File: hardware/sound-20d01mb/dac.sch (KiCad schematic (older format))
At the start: 18 parts

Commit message: THT to SMD Capacitor
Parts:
- C?: footprint Capacitor_THT:CP_Radial_D8.0mm_P3.50mm -> Capacitor_SMD:CP_Elec_4x5.4
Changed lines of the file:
@@
 F 0 "C?" H 3468 4846 50  0000 L CNN
 F 1 "10uF" H 3468 4755 50  0000 L CNN
-F 2 "Capacitor_THT:CP_Radial_D8.0mm_P3.50mm" H 3388 4650 50  0001 C CNN
+F 2 "Capacitor_SMD:CP_Elec_4x5.4" H 3388 4650 50  0001 C CNN
 F 3 "~" H 3350 4800 50  0001 C CNN
 	1    3350 4800

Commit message: Added AD1938
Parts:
- removed C? (x2): 2.2uF, Capacitor_SMD:C_1206_3216Metric_Pad1.42x1.75mm_HandSolder, symbol Device:C
- removed C?: 10uF, Capacitor_THT:CP_Radial_D8.0mm_P3.50mm, symbol Device:CP
- removed C? (x2): 0.1uF, Capacitor_SMD:C_1206_3216Metric_Pad1.42x1.75mm_HandSolder, symbol Device:C
- removed U?: PCM5102A, Package_SO:TSSOP-20_4.4x6.5mm_P0.65mm, symbol sound-20d01_Library:PCM5102A
- added U?: AD1938, Package_QFP:LQFP-48_7x7mm_P0.5mm, symbol sound-20d01_Library:AD1938
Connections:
- wire segments 94 -> 44
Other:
- moved on the sheet: C?

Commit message: Updated schematics
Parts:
- added C?: 10uF, Capacitor_SMD:CP_Elec_4x5.4, symbol Device:CP
- added C? (x2): 0.1uF, Capacitor_SMD:C_1206_3216Metric_Pad1.42x1.75mm_HandSolder, symbol Device:C
- added C?: 47uF, symbol Device:CP
- added C?: 5.6nF, symbol Device:C
- added C?: 390pF, symbol Device:C
- added R?: 562R, symbol Device:R
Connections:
- net labels added: DAC_CM, DAC_FILTR, DAC_LF
- wire segments 44 -> 95
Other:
- moved on the sheet: C?, R?, U?

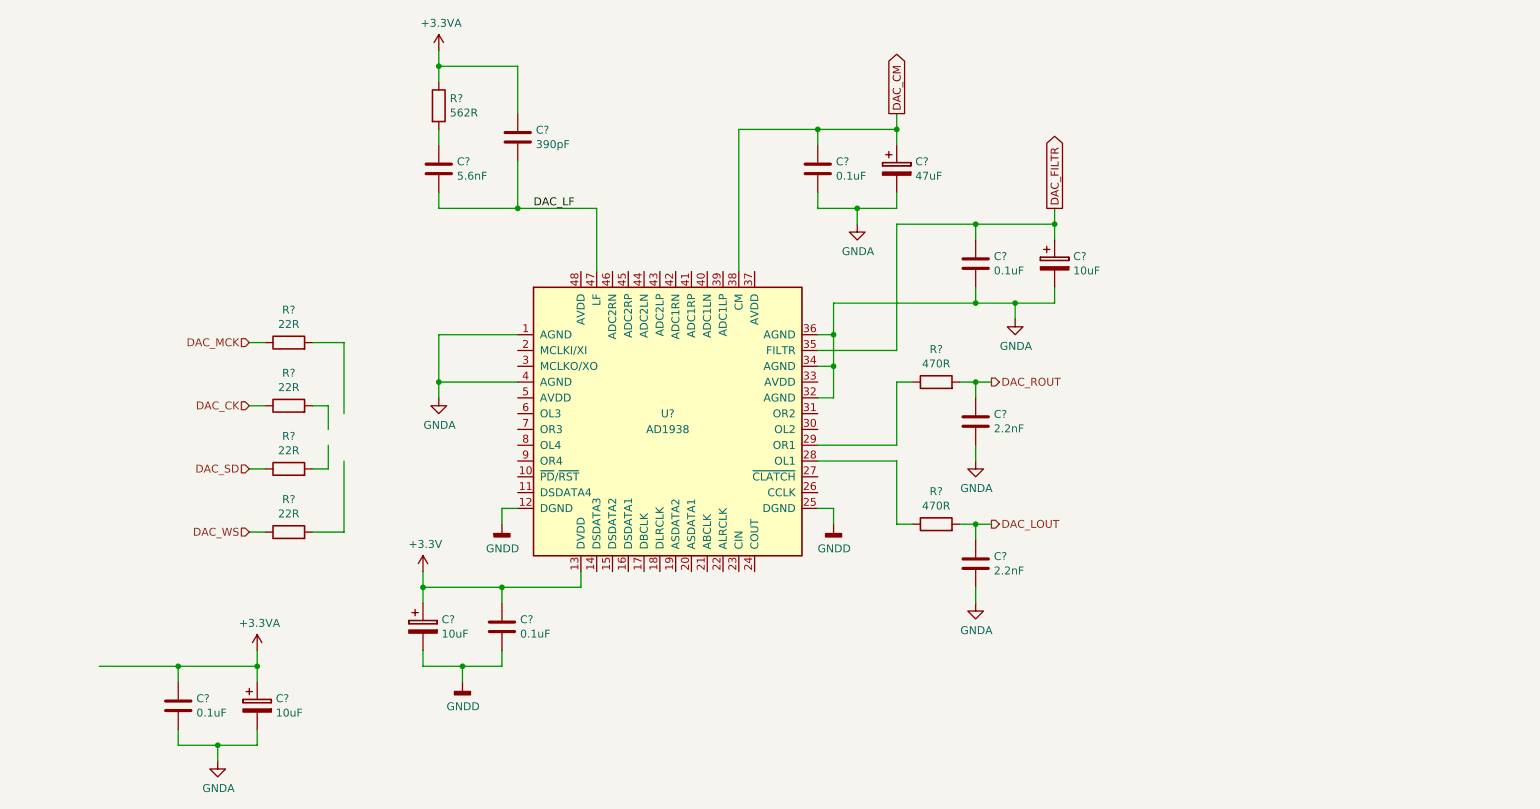
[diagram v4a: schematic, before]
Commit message: Added PCM5142
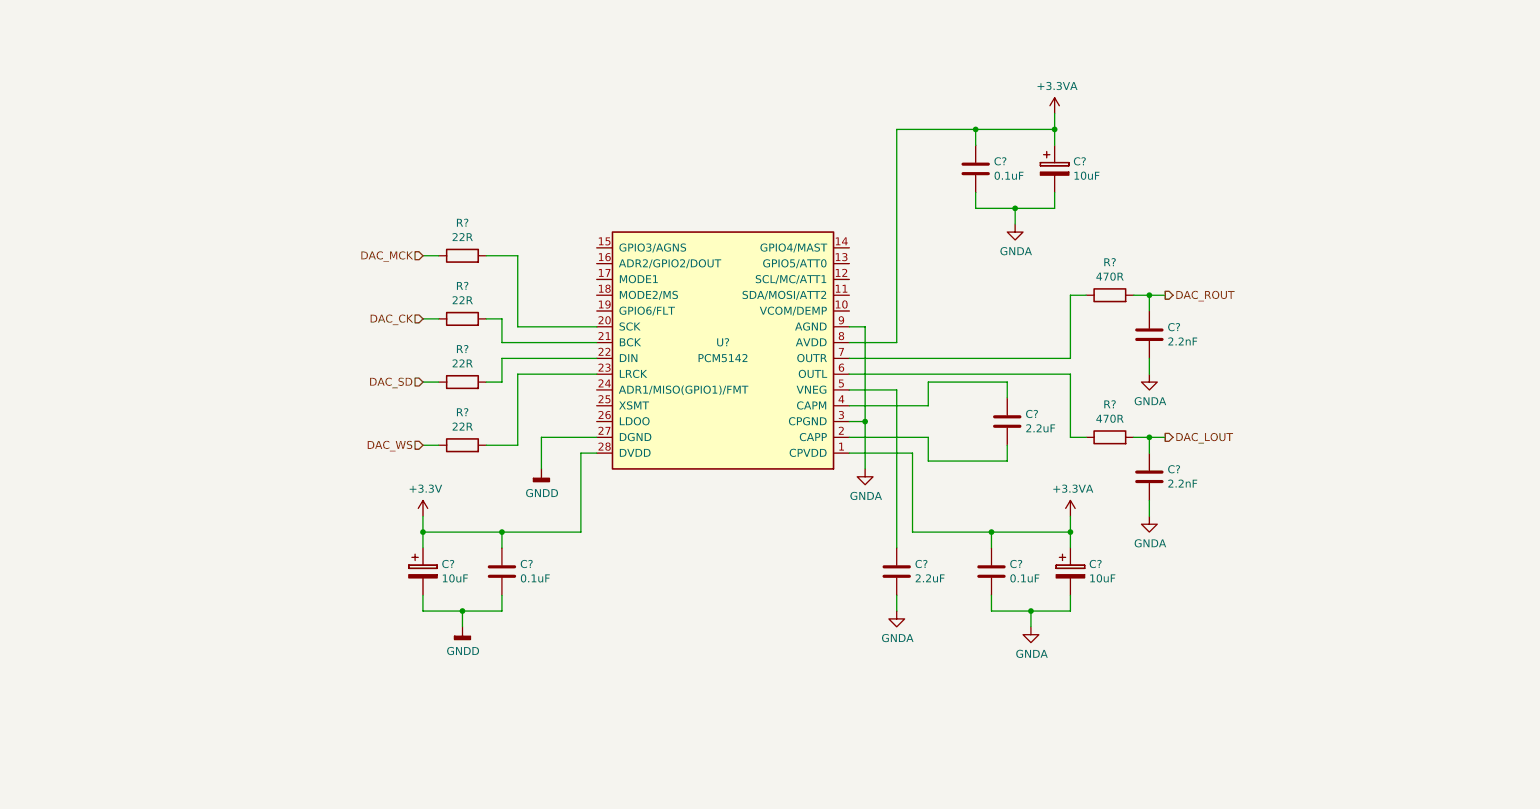
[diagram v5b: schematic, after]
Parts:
- removed C?: 10uF, Capacitor_SMD:CP_Elec_4x5.4, symbol Device:CP
- removed C? (x2): 0.1uF, Capacitor_SMD:C_1206_3216Metric_Pad1.42x1.75mm_HandSolder, symbol Device:C
- removed C?: 47uF, symbol Device:CP
- removed C?: 5.6nF, symbol Device:C
- removed C?: 390pF, symbol Device:C
- removed R?: 562R, symbol Device:R
- removed U?: AD1938, Package_QFP:LQFP-48_7x7mm_P0.5mm, symbol sound-20d01_Library:AD1938
- added C? (x2): 2.2uF, Capacitor_SMD:C_1206_3216Metric_Pad1.42x1.75mm_HandSolder, symbol Device:C
- added C?: 10uF, Capacitor_THT:CP_Radial_D8.0mm_P3.50mm, symbol Device:CP
- added C?: 0.1uF, Capacitor_SMD:C_1206_3216Metric_Pad1.42x1.75mm_HandSolder, symbol Device:C
- added U?: PCM5142, Package_SO:TSSOP-28_4.4x9.7mm_P0.65mm, symbol sound-20d01_Library:PCM5142
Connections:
- net labels removed: DAC_CM, DAC_FILTR, DAC_LF
- wire segments 95 -> 83
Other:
- moved on the sheet: C?, R?

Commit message: Added I2C Volume control
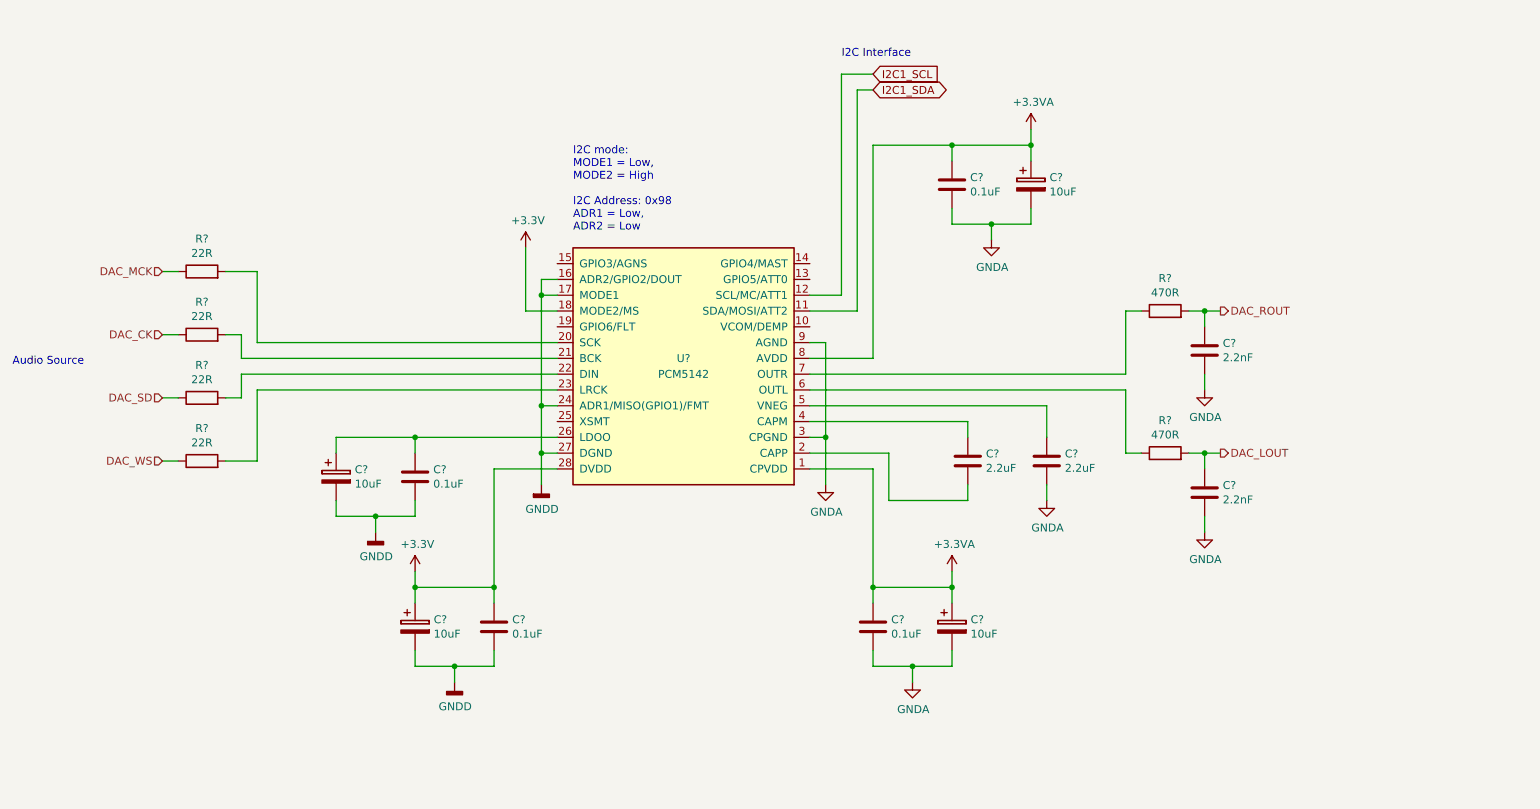
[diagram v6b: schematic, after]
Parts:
- added C?: 10uF, Capacitor_SMD:CP_Elec_4x5.4, symbol Device:CP
- added C?: 0.1uF, Capacitor_SMD:C_1206_3216Metric_Pad1.42x1.75mm_HandSolder, symbol Device:C
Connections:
- net +3V3: now also U?.18 (MODE2/MS)
- net GNDD: now also U?.16 (ADR2/GPIO2/DOUT), U?.17 (MODE1), U?.24 (ADR1/MISO(GPIO1)/FMT), C?.2, C?.2
- net I2C1_SDA: now reaches U?.11 (SDA/MOSI/ATT2)
- net I2C1_SCL: now reaches U?.12 (SCL/MC/ATT1)
- net at U?.26 (LDOO): now also C?.1, C?.1
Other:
- note added: "Audio Source"
- note added: "I2C Interface"
- note added: "I2C mode:\nMODE1 = Low,\nMODE2 = High\n\nI2C Address: 0x98\nADR1 = Low,\nADR2 = Low"
- moved on the sheet: C?, R?, U?

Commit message: Updated PSU and DAC
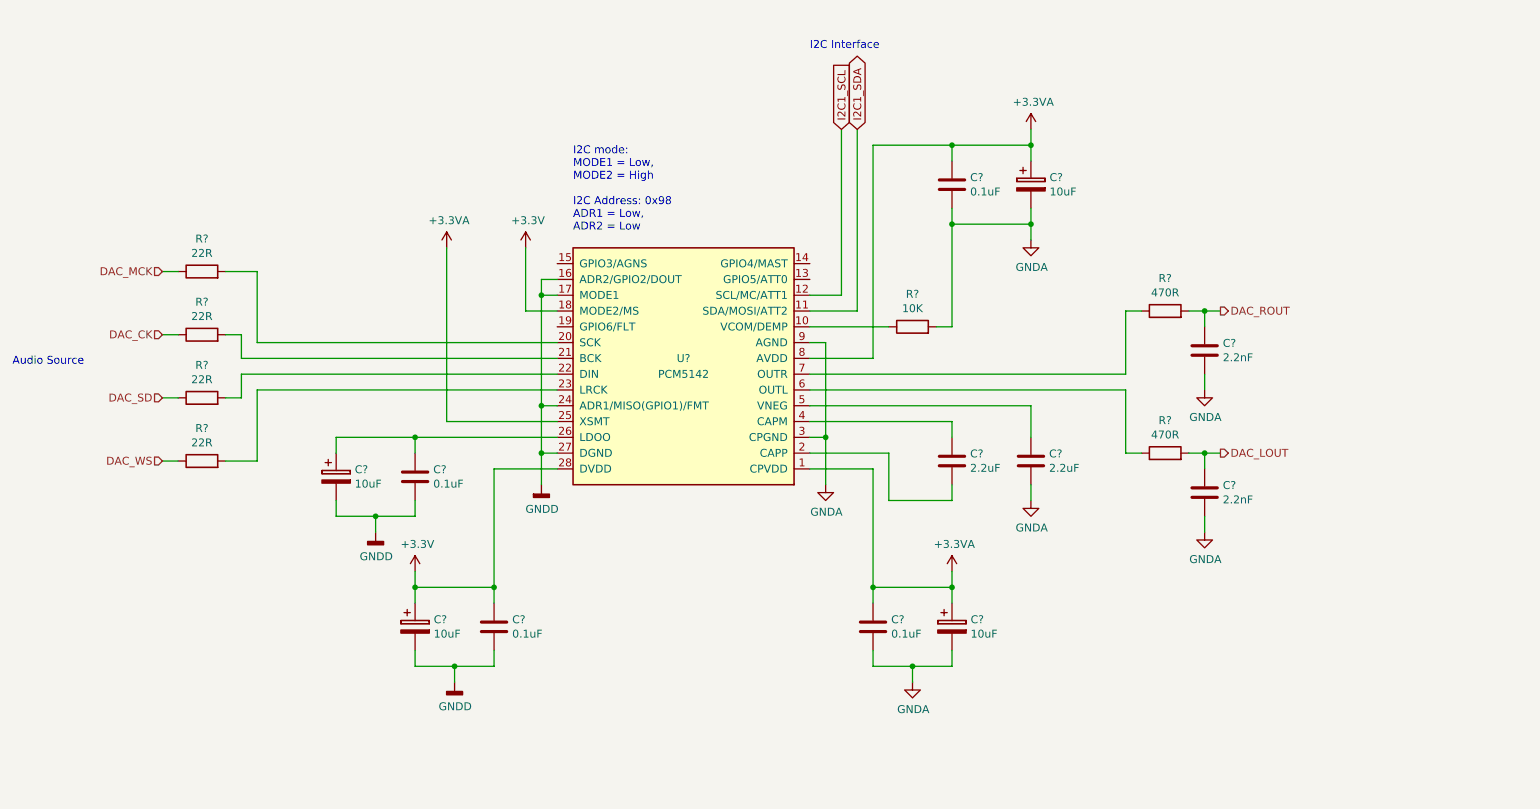
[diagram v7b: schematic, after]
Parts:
- added R?: 10K, Resistor_SMD:R_1206_3216Metric_Pad1.42x1.75mm_HandSolder, symbol Device:R
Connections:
- net +3.3VA: now also U?.25 (XSMT)
- net GNDA: now also R?.2
- net at U?.10 (VCOM/DEMP): now also R?.1
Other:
- moved on the sheet: C?
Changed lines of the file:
@@
 L Device:C C?
 U 1 1 6142C574
-P 7300 3950
+P 7200 3950
 AR Path="/60DE2DF4/6142C574" Ref="C?"  Part="1"
 AR Path="/60DE2DF1/6142C574" Ref="C?"  Part="1"
-F 0 "C?" H 7415 3996 50  0000 L CNN
-F 1 "2.2uF" H 7415 3905 50  0000 L CNN
-F 2 "Capacitor_SMD:C_1206_3216Metric_Pad1.42x1.75mm_HandSolder" H 7338 3800 50  0001 C CNN
-F 3 "~" H 7300 3950 50  0001 C CNN
-	1    7300 3950
+F 0 "C?" H 7315 3996 50  0000 L CNN
+F 1 "2.2uF" H 7315 3905 50  0000 L CNN
+F 2 "Capacitor_SMD:C_1206_3216Metric_Pad1.42x1.75mm_HandSolder" H 7238 3800 50  0001 C CNN
+F 3 "~" H 7200 3950 50  0001 C CNN
+	1    7200 3950
 	1    0    0    -1
 $EndComp
@@
 	6800 4200 6800 3900
 Wire Wire Line
-	6800 4200 7300 4200
-Wire Wire Line
-	7300 3800 7300 3700
-Wire Wire Line
-	7300 4100 7300 4200
+	6800 4200 7200 4200
+Wire Wire Line
+	7200 3800 7200 3700
+Wire Wire Line
+	7200 4100 7200 4200
 Wire Wire Line
 	6300 3800 6400 3800
@@
 L Device:C C?
 U 1 1 614356A2
-P 7800 3950
+P 7700 3950
 AR Path="/60DE2DF4/614356A2" Ref="C?"  Part="1"
 AR Path="/60DE2DF1/614356A2" Ref="C?"  Part="1"
-F 0 "C?" H 7915 3996 50  0000 L CNN
-F 1 "2.2uF" H 7915 3905 50  0000 L CNN
-F 2 "Capacitor_SMD:C_1206_3216Metric_Pad1.42x1.75mm_HandSolder" H 7838 3800 50  0001 C CNN
-F 3 "~" H 7800 3950 50  0001 C CNN
-	1    7800 3950
+F 0 "C?" H 7815 3996 50  0000 L CNN
+F 1 "2.2uF" H 7815 3905 50  0000 L CNN
+F 2 "Capacitor_SMD:C_1206_3216Metric_Pad1.42x1.75mm_HandSolder" H 7738 3800 50  0001 C CNN
+F 3 "~" H 7700 3950 50  0001 C CNN
+	1    7700 3950
 	1    0    0    -1
 $EndComp
@@
 	6700 4000 6700 4750
 Wire Wire Line
-	7800 4100 7800 4200
+	7700 4100 7700 4200
 $Comp
 L Device:CP C?
@@
 	7700 1950 7700 1850
 Wire Wire Line
-	7450 2450 7700 2450
-Wire Wire Line
-	7200 2450 7450 2450
-Connection ~ 7450 2450
-Wire Wire Line
-	7450 2450 7450 2550
+	7700 2450 7700 2550
 $Comp
 L power:GNDA #PWR?
 U 1 1 6143EA16
-P 7450 2550
-F 0 "#PWR?" H 7450 2300 50  0001 C CNN
-F 1 "GNDA" H 7455 2377 50  0000 C CNN
-F 2 "" H 7450 2550 50  0001 C CNN
-F 3 "" H 7450 2550 50  0001 C CNN
-	1    7450 2550
+P 7700 2550
+F 0 "#PWR?" H 7700 2300 50  0001 C CNN
+F 1 "GNDA" H 7705 2377 50  0000 C CNN
+F 2 "" H 7700 2550 50  0001 C CNN
+F 3 "" H 7700 2550 50  0001 C CNN
+	1    7700 2550
 	1    0    0    -1
 $EndComp
@@
 L power:GNDA #PWR?
 U 1 1 6143D42A
-P 7800 4200
-F 0 "#PWR?" H 7800 3950 50  0001 C CNN
-F 1 "GNDA" H 7805 4027 50  0000 C CNN
-F 2 "" H 7800 4200 50  0001 C CNN
-F 3 "" H 7800 4200 50  0001 C CNN
-	1    7800 4200
+P 7700 4200
+F 0 "#PWR?" H 7700 3950 50  0001 C CNN
+F 1 "GNDA" H 7705 4027 50  0000 C CNN
+F 2 "" H 7700 4200 50  0001 C CNN
+F 3 "" H 7700 4200 50  0001 C CNN
+	1    7700 4200
 	1    0    0    -1
 $EndComp
@@
 	4300 4000 4300 4750
 Wire Wire Line
-	6300 3700 7300 3700
-Wire Wire Line
-	6300 3600 7800 3600
-Wire Wire Line
-	7800 3600 7800 3800
+	6300 3700 7200 3700
+Wire Wire Line
+	7700 3600 7700 3800
 Connection ~ 6700 4750
 Connection ~ 4300 4750
@@
 Wire Wire Line
 	6300 3300 6700 3300
-Text GLabel 6700 1600 2    50   BiDi ~ 0
+Text GLabel 6600 1850 1    50   BiDi ~ 0
 I2C1_SDA
-Text GLabel 6700 1500 2    50   Input ~ 0
+Text GLabel 6500 1850 1    50   Input ~ 0
 I2C1_SCL
 Wire Wire Line
@@
 Audio Source
 Wire Wire Line
-	6600 3000 6600 1600
+	6600 3000 6600 1850
 Wire Wire Line
 	6300 3000 6600 3000
 Wire Wire Line
-	6500 1500 6500 2900
-Wire Wire Line
-	6600 1600 6700 1600
-Wire Wire Line
-	6500 1500 6700 1500
-Text Notes 6500 1400 0    50   ~ 0
+	6500 1850 6500 2900
+Text Notes 6300 1350 0    50   ~ 0
 I2C Interface
 Wire Wire Line
@@
 Wire Wire Line
 	4600 3600 4600 3900
+$Comp
+L Device:R R?
+U 1 1 6147608B
+P 6950 3100
+F 0 "R?" V 7157 3100 50  0000 C CNN
+F 1 "10K" V 7066 3100 50  0000 C CNN
+F 2 "Resistor_SMD:R_1206_3216Metric_Pad1.42x1.75mm_HandSolder" V 6880 3100 50  0001 C CNN
+F 3 "~" H 6950 3100 50  0001 C CNN
+	1    6950 3100
+	0    -1   -1   0
+$EndComp
+Wire Wire Line
+	6300 3100 6800 3100
+Wire Wire Line
+	7100 3100 7200 3100
+Wire Wire Line
+	7200 3100 7200 2450
+Connection ~ 7200 2450
+$Comp
+L power:+3.3VA #PWR?
+U 1 1 61486380
+P 4000 2600
+F 0 "#PWR?" H 4000 2450 50  0001 C CNN
+F 1 "+3.3VA" H 4015 2773 50  0000 C CNN
+F 2 "" H 4000 2600 50  0001 C CNN
+F 3 "" H 4000 2600 50  0001 C CNN
+	1    4000 2600
+	1    0    0    -1
+$EndComp
+Wire Wire Line
+	4700 3700 4000 3700
+Wire Wire Line
+	4000 3700 4000 2600
+Wire Wire Line
+	6300 3600 7700 3600
+Connection ~ 7700 2450
+Wire Wire Line
+	7200 2450 7700 2450
 $EndSCHEMATC

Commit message: Added DAC GPIO
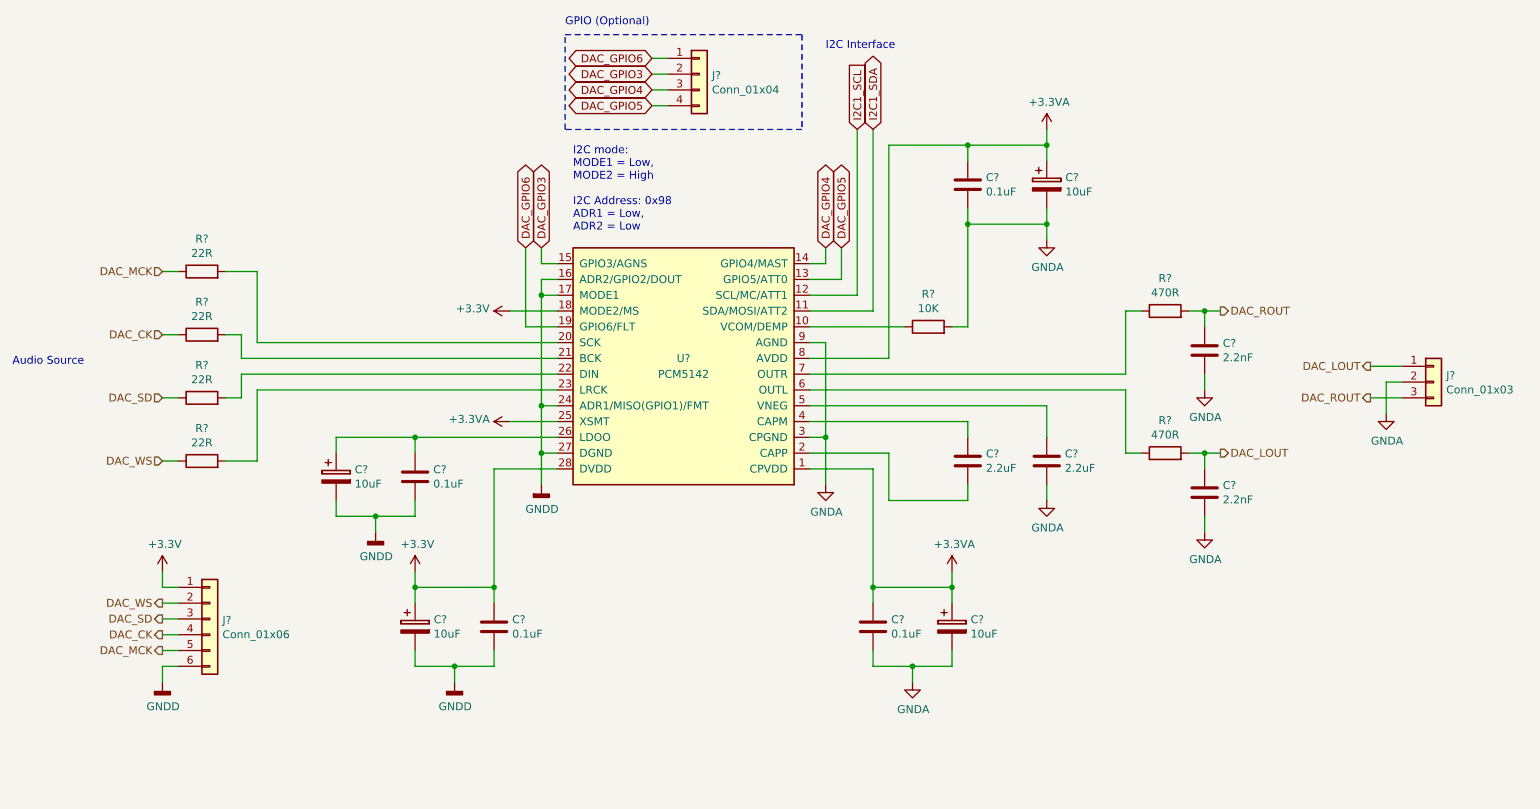
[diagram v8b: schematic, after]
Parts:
- added J?: Conn_01x06, Connector_PinHeader_2.54mm:PinHeader_1x06_P2.54mm_Vertical, symbol Connector_Generic:Conn_01x06
- added J?: Conn_01x03, Connector_PinHeader_2.54mm:PinHeader_1x03_P2.54mm_Vertical, symbol Connector_Generic:Conn_01x03
- added J?: Conn_01x04, Connector_PinHeader_2.54mm:PinHeader_1x04_P2.54mm_Vertical, symbol Connector_Generic:Conn_01x04
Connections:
- net +3V3: now also J?.1 (Pin_1)
- net DAC_CK: now also J?.4 (Pin_4)
- net DAC_LOUT: now also J?.1 (Pin_1)
- net DAC_MCK: now also J?.5 (Pin_5)
- net DAC_ROUT: now also J?.3 (Pin_3)
- net DAC_SD: now also J?.3 (Pin_3)
- net DAC_WS: now also J?.2 (Pin_2)
- net GNDA: now also J?.2 (Pin_2)
- net GNDD: now also J?.6 (Pin_6)
- net DAC_GPIO5: now reaches U?.13 (GPIO5/ATT0)
- net DAC_GPIO5: now also J?.4 (Pin_4)
- net DAC_GPIO4: now reaches U?.14 (GPIO4/MAST)
- net DAC_GPIO4: now also J?.3 (Pin_3)
- net DAC_GPIO3: now reaches U?.15 (GPIO3/AGNS)
- net DAC_GPIO3: now also J?.2 (Pin_2)
- net DAC_GPIO6: now reaches U?.19 (GPIO6/FLT)
- net DAC_GPIO6: now also J?.1 (Pin_1)
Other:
- note added: "GPIO (Optional)"
- moved on the sheet: C?, R?
